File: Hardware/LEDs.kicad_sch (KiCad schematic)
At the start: 129 parts

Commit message: Final design for v2.0
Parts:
- added D131, D132, D133: WS2812B, LED_SMD:LED_WS2812B-2020_PLCC4_2.0x2.0mm, symbol LED:WS2812B
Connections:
- net +5V: now also D131.1 (VDD), D132.1 (VDD), D133.1 (VDD); no longer D280.1 (VDD)
- net GND: now also D131.3 (VSS), D132.3 (VSS), D133.3 (VSS); no longer D280.3 (VSS)
- net at D280.2 (DOUT): no longer D281.4 (DIN)
- net LED_BK: now reaches D263.4 (DIN)
- net LED_BK: now also D133.2 (DOUT); no longer D262.2 (DOUT)
- new net: D131.2 (DOUT), D132.4 (DIN)
- new net: D132.2 (DOUT), D133.4 (DIN)
- new net LED_BR: D131.4 (DIN), D262.2 (DOUT)
- no-connect marks 0 -> 1
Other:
- note added: "Lock Indicators"
- moved on the sheet: D263, D264, D265, D266, D267, D268, D269, D270, D271, D272, D273, D274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

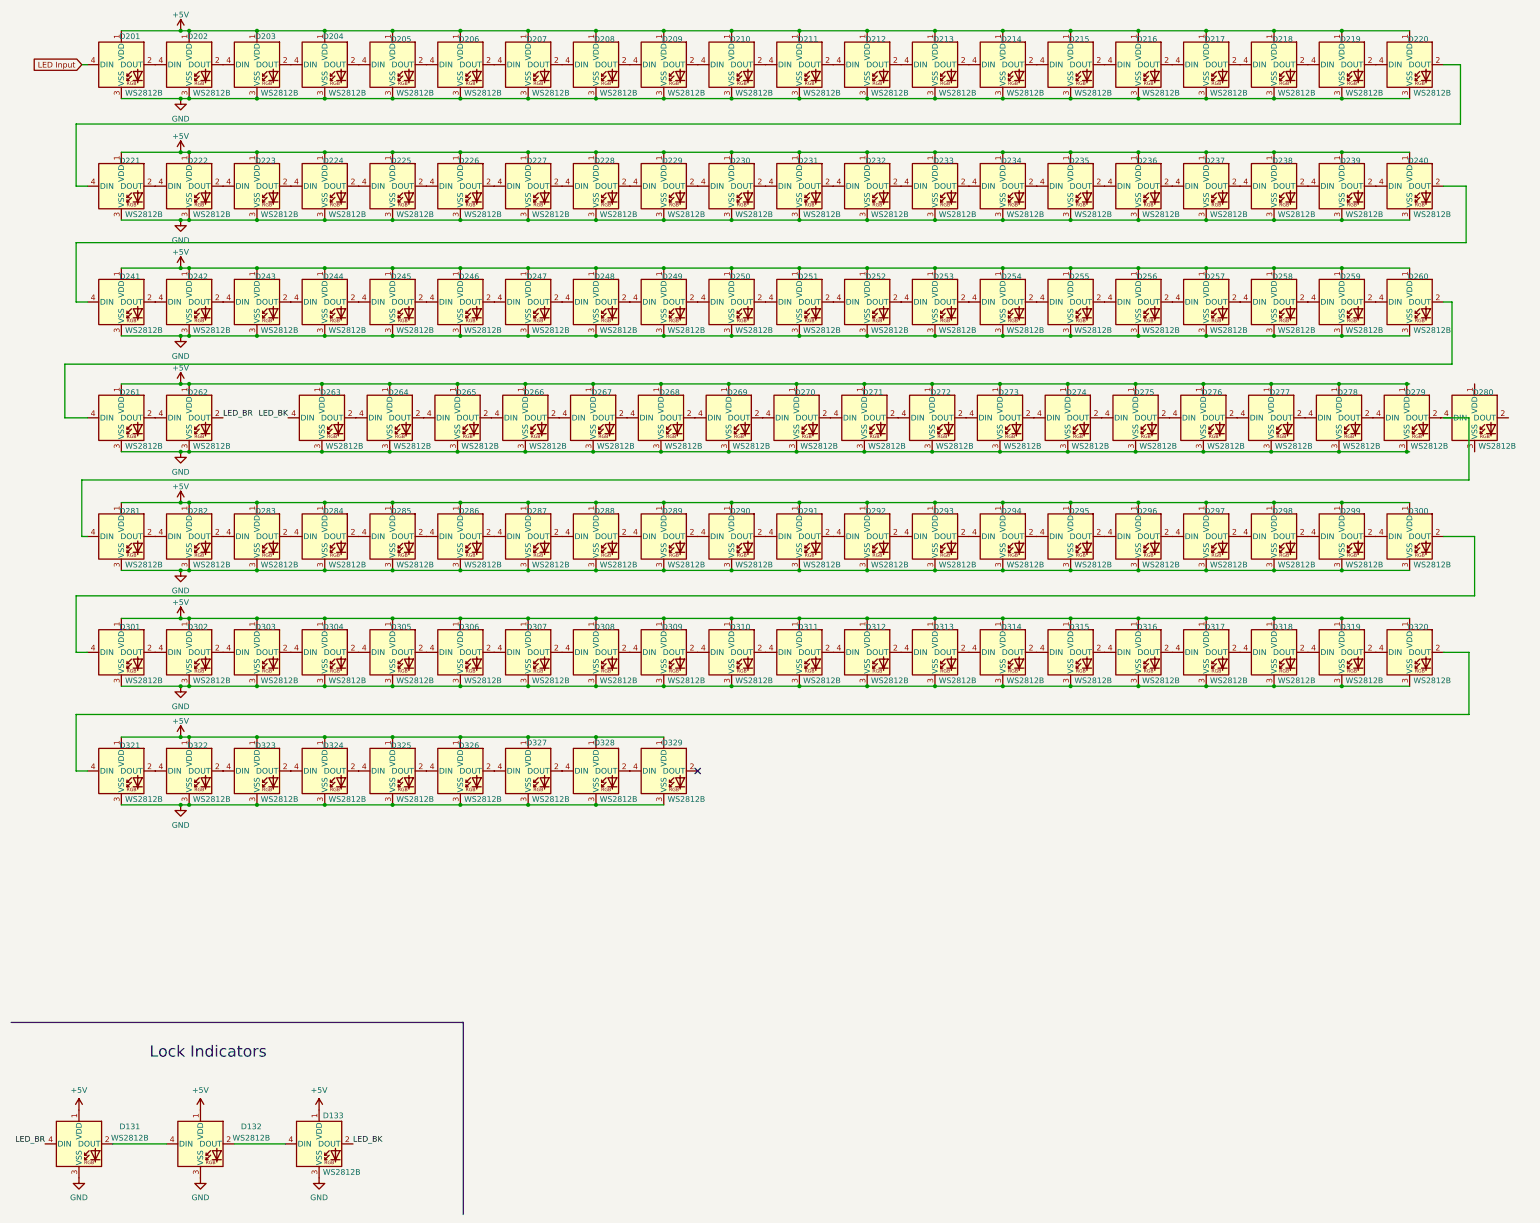
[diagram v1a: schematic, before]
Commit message: Increment to Rev 2.1, Fix Lock Indicators, Repair Ground Connection D280, move covered mount hole.
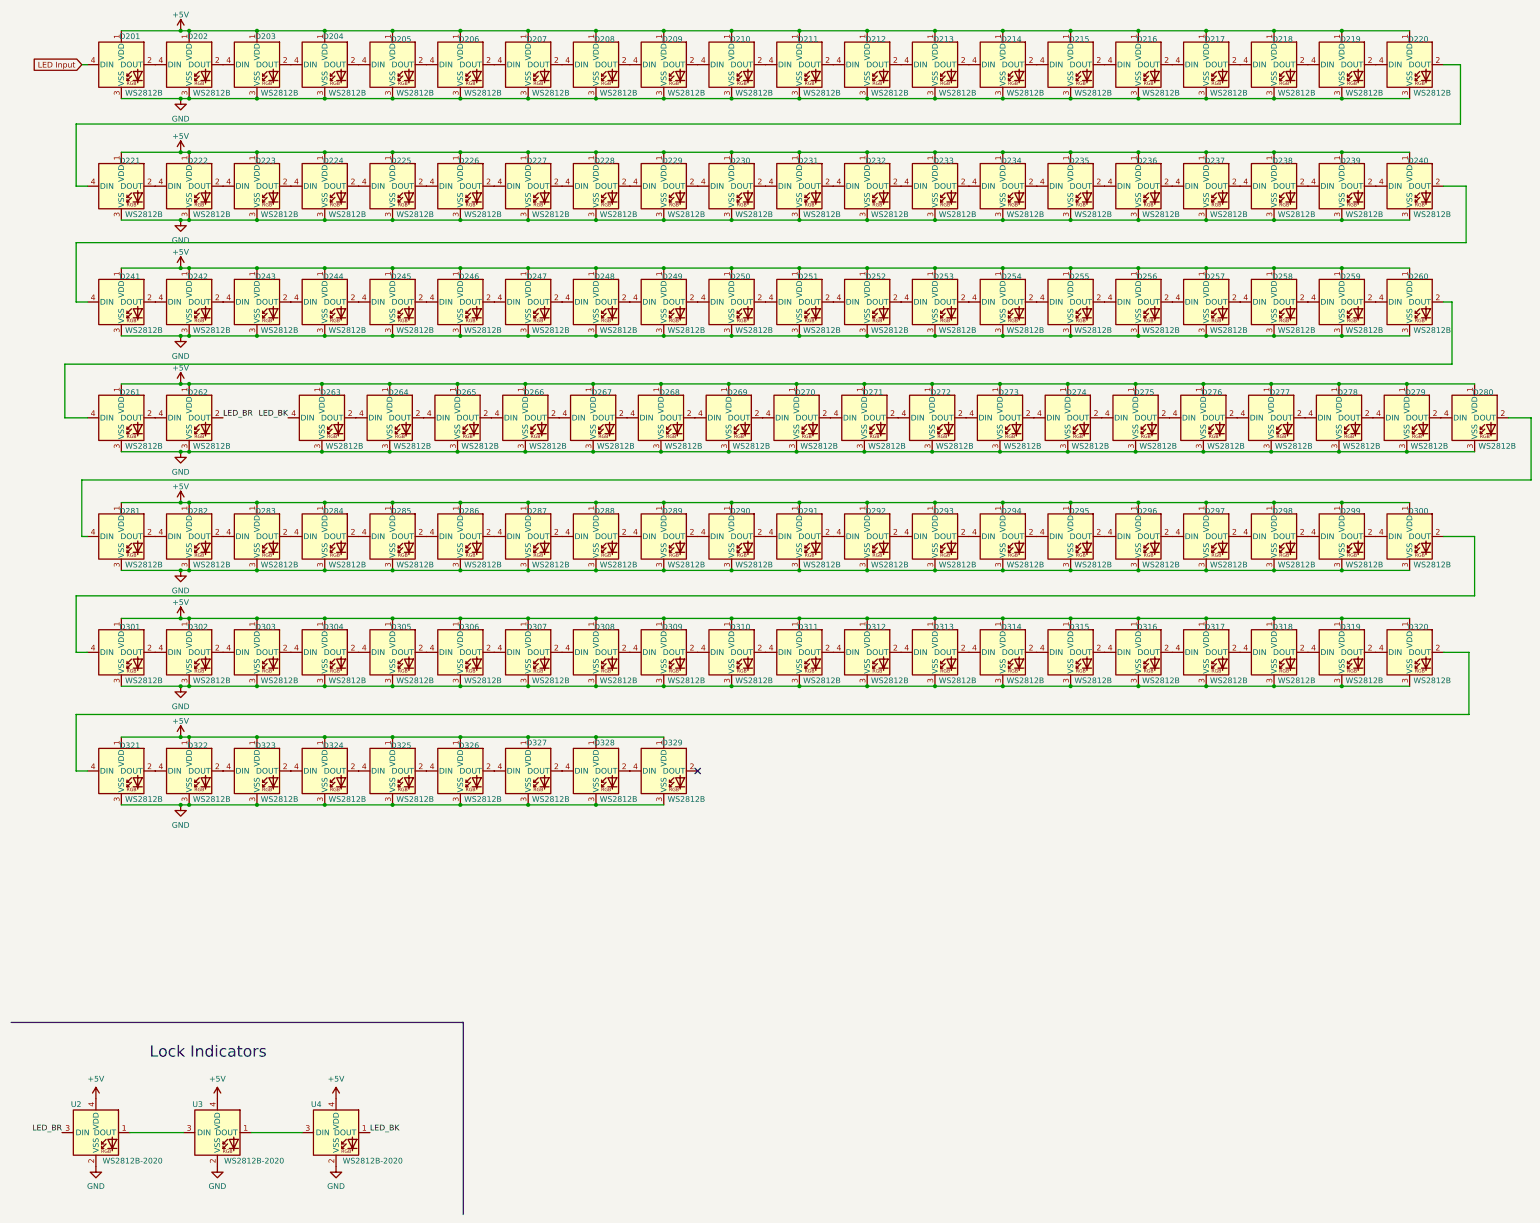
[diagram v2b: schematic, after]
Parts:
- removed D131, D132, D133: WS2812B, LED_SMD:LED_WS2812B-2020_PLCC4_2.0x2.0mm, symbol LED:WS2812B
- added U2, U3, U4: WS2812B-2020, LED_SMD:LED_WS2812B-2020_PLCC4_2.0x2.0mm, symbol WS2812:WS2812B-2020
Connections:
- net +5V: now also D280.1 (VDD), U2.4 (VDD), U3.4 (VDD), U4.4 (VDD)
- net GND: now also D280.3 (VSS), U2.2 (VSS), U3.2 (VSS), U4.2 (VSS)
- net LED_BK: now also U4.1 (DOUT)
- net LED_BR: now also U2.3 (DIN)
- net at D280.2 (DOUT): now also D281.4 (DIN)
- new net: U3.1 (DOUT), U4.3 (DIN)
- new net: U2.1 (DOUT), U3.3 (DIN)
